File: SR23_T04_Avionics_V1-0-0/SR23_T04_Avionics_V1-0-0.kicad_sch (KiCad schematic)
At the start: 46 parts, among them J1 QWIIC, J11 Conn_01x02, J12 Conn_01x02, J13 Conn_01x02, J14 BAT_CHARGE, J2 QWIIC, J3 QWIIC, J4 BAT_POWER, J5 BAT_uC, J6 BAT_PCB+, J7 Conn_01x03, J8 Conn_01x03, J9 Conn_01x03, Q2 BSP75N, Q3 BSP75N, Q4 BSP75N, SW1 SW_DIP_x02, U1 MCP73831-2-OT, U2 MS563702BA03-50, U3 MPU-6050, U4 MOUDLE-SEEEDUINO-XIAO-ESP32C3

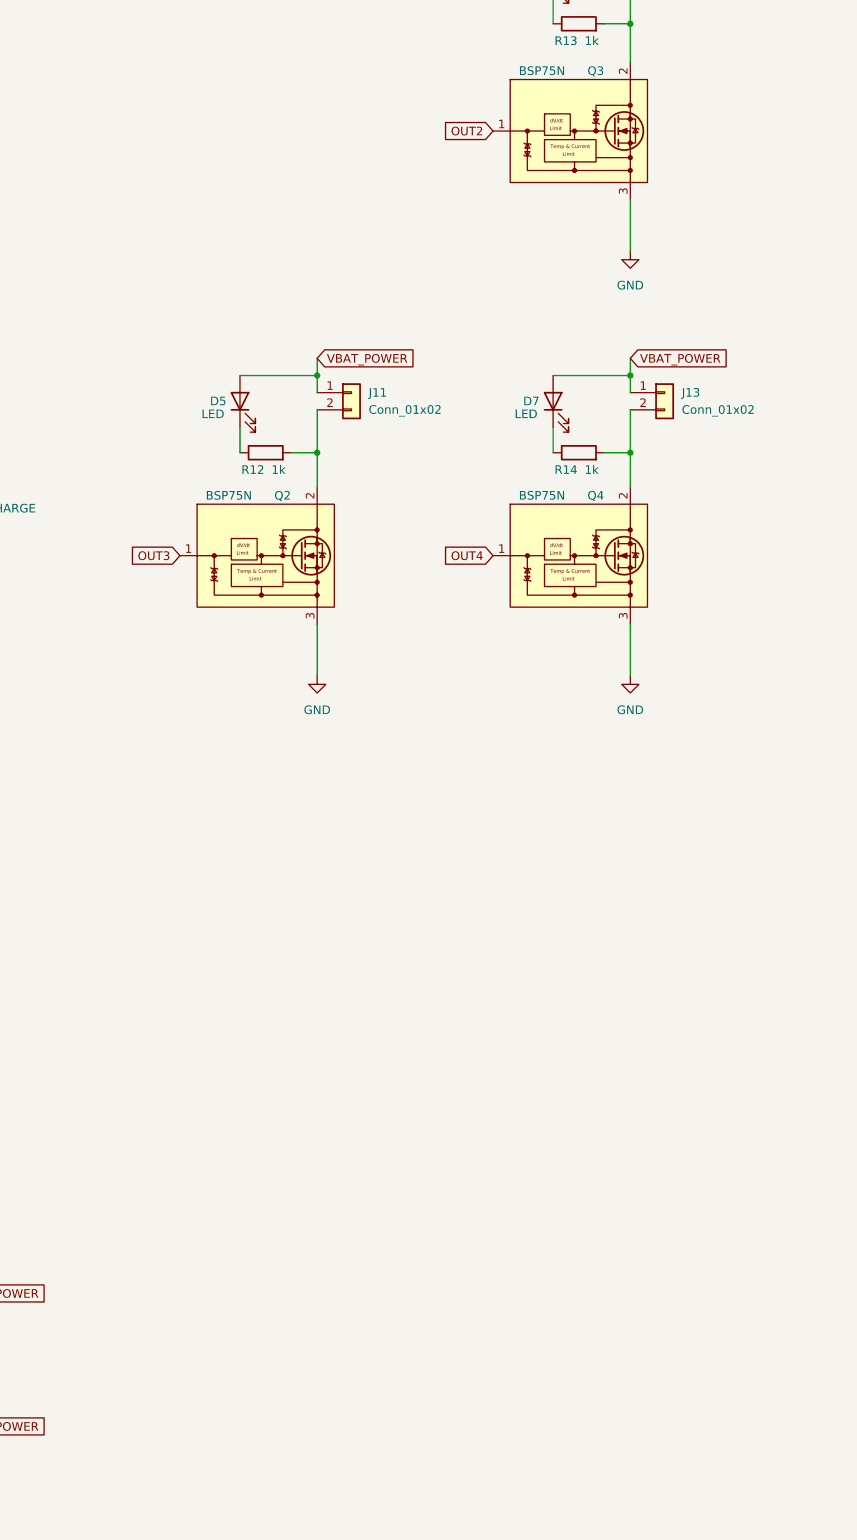
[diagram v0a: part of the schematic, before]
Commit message: wip: rooting of the board completed - waiting on review
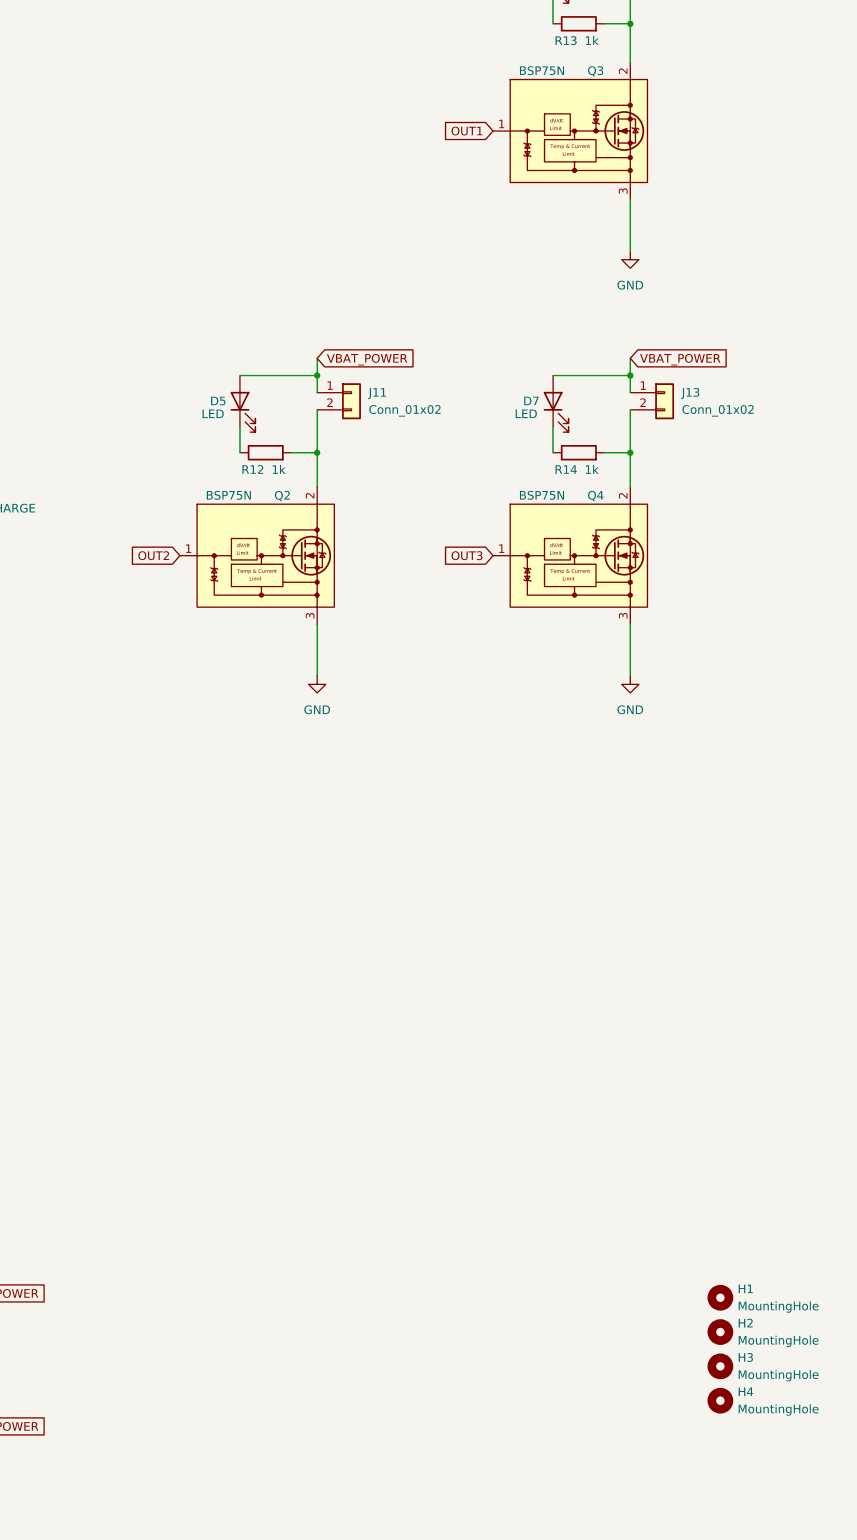
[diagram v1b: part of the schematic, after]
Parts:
- added H1, H2, H3, H4: MountingHole, MountingHole:MountingHole_3.2mm_M3_ISO7380, symbol Mechanical:MountingHole
- J14: footprint Connector_JST:JST_XH_S2B-XH-A-1_1x02_P2.50mm_Horizontal -> Connector_PinHeader_2.54mm:PinHeader_2x01_P2.54mm_Vertical
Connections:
- net OUT1: now also Q3.1 (G)
- net OUT2: now also Q2.1 (G); no longer Q3.1 (G)
- net OUT3: now also Q4.1 (G); no longer Q2.1 (G)
- net OUT4: no longer Q4.1 (G)
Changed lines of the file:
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@@
     )
   )
-  (global_label "OUT3" (shape input) (at 309.88 113.665 180) (fields_autoplaced)
+  (global_label "OUT2" (shape input) (at 309.88 113.665 180) (fields_autoplaced)
     (effects (font (size 1.27 1.27)) (justify right))
     (property "Intersheet References" "${INTERSHEET_REFS}" (id 0) (at 302.6288 113.5856 0)
@@
     )
   )
-  (global_label "OUT2" (shape input) (at 356.235 50.8 180) (fields_autoplaced)
+  (global_label "OUT1" (shape input) (at 356.235 50.8 180) (fields_autoplaced)
     (effects (font (size 1.27 1.27)) (justify right))
     (property "Intersheet References" "${INTERSHEET_REFS}" (id 0) (at 348.9838 50.7206 0)
@@
     )
   )
-  (global_label "OUT4" (shape input) (at 356.235 113.665 180) (fields_autoplaced)
+  (global_label "OUT3" (shape input) (at 356.235 113.665 180) (fields_autoplaced)
     (effects (font (size 1.27 1.27)) (justify right))
     (property "Intersheet References" "${INTERSHEET_REFS}" (id 0) (at 348.9838 113.5856 0)
@@
       (effects (font (size 1.27 1.27)) (justify right))
     )
-    (property "Footprint" "Connector_JST:JST_XH_S2B-XH-A-1_1x02_P2.50mm_Horizontal" (id 2) (at 271.78 105.41 0)
+    (property "Footprint" "Connector_PinHeader_2.54mm:PinHeader_2x01_P2.54mm_Vertical" (id 2) (at 271.78 105.41 0)
       (effects (font (size 1.27 1.27)) hide)
     )
@@
     (pin "1")
   )
+  (symbol (lib_id "Mechanical:MountingHole") (at 389.89 223.52 0) (unit 1)
+    (in_bom yes) (on_board yes) (fields_autoplaced)
+    (property "Reference" "H1" (id 0) (at 392.43 222.2499 0)
+      (effects (font (size 1.27 1.27)) (justify left))
+    )
+    (property "Value" "MountingHole" (id 1) (at 392.43 224.7899 0)
+      (effects (font (size 1.27 1.27)) (justify left))
+    )
+    (property "Footprint" "MountingHole:MountingHole_3.2mm_M3_ISO7380" (id 2) (at 389.89 223.52 0)
+      (effects (font (size 1.27 1.27)) hide)
+    )
+    (property "Datasheet" "~" (id 3) (at 389.89 223.52 0)
+      (effects (font (size 1.27 1.27)) hide)
+    )
+  )
   (symbol (lib_id "Connector_Generic:Conn_01x02") (at 175.26 199.39 90) (unit 1)
     (in_bom yes) (on_board yes) (fields_autoplaced)
@@
     (pin "1")
     (pin "2")
+  )
+  (symbol (lib_id "Mechanical:MountingHole") (at 389.89 228.6 0) (unit 1)
+    (in_bom yes) (on_board yes) (fields_autoplaced)
+    (property "Reference" "H2" (id 0) (at 392.43 227.3299 0)
+      (effects (font (size 1.27 1.27)) (justify left))
+    )
+    (property "Value" "MountingHole" (id 1) (at 392.43 229.8699 0)
+      (effects (font (size 1.27 1.27)) (justify left))
+    )
+    (property "Footprint" "MountingHole:MountingHole_3.2mm_M3_ISO7380" (id 2) (at 389.89 228.6 0)
+      (effects (font (size 1.27 1.27)) hide)
+    )
+    (property "Datasheet" "~" (id 3) (at 389.89 228.6 0)
+      (effects (font (size 1.27 1.27)) hide)
+    )
   )
   (symbol (lib_id "Device:R") (at 168.91 133.35 180) (unit 1)
@@
     (pin "2")
   )
+  (symbol (lib_id "Mechanical:MountingHole") (at 389.89 233.68 0) (unit 1)
+    (in_bom yes) (on_board yes) (fields_autoplaced)
+    (property "Reference" "H3" (id 0) (at 392.43 232.4099 0)
+      (effects (font (size 1.27 1.27)) (justify left))
+    )
+    (property "Value" "MountingHole" (id 1) (at 392.43 234.9499 0)
+      (effects (font (size 1.27 1.27)) (justify left))
+    )
+    (property "Footprint" "MountingHole:MountingHole_3.2mm_M3_ISO7380" (id 2) (at 389.89 233.68 0)
+      (effects (font (size 1.27 1.27)) hide)
+    )
+    (property "Datasheet" "~" (id 3) (at 389.89 233.68 0)
+      (effects (font (size 1.27 1.27)) hide)
+    )
+  )
   (symbol (lib_id "power:GND") (at 119.38 177.165 0) (unit 1)
     (in_bom yes) (on_board yes) (fields_autoplaced)
@@
     )
     (pin "1")
+  )
+  (symbol (lib_id "Mechanical:MountingHole") (at 389.89 238.76 0) (unit 1)
+    (in_bom yes) (on_board yes) (fields_autoplaced)
+    (property "Reference" "H4" (id 0) (at 392.43 237.4899 0)
+      (effects (font (size 1.27 1.27)) (justify left))
+    )
+    (property "Value" "MountingHole" (id 1) (at 392.43 240.0299 0)
+      (effects (font (size 1.27 1.27)) (justify left))
+    )
+    (property "Footprint" "MountingHole:MountingHole_3.2mm_M3_ISO7380" (id 2) (at 389.89 238.76 0)
+      (effects (font (size 1.27 1.27)) hide)
+    )
+    (property "Datasheet" "~" (id 3) (at 389.89 238.76 0)
+      (effects (font (size 1.27 1.27)) hide)
+    )
   )
   (symbol (lib_id "MS5037:MS563702BA03-50") (at 67.945 43.815 0) (unit 1)
@@
       (reference "D7") (unit 1) (value "LED") (footprint "LED_SMD:LED_0201_0603Metric_Pad0.64x0.40mm_HandSolder")
     )
+    (path "/298485de-c642-478c-8067-8a5d032e90c1"
+      (reference "H1") (unit 1) (value "MountingHole") (footprint "MountingHole:MountingHole_3.2mm_M3_ISO7380")
+    )
+    (path "/42218edd-ae1c-462d-a3bd-fe78546cce83"
+      (reference "H2") (unit 1) (value "MountingHole") (footprint "MountingHole:MountingHole_3.2mm_M3_ISO7380")
+    )
+    (path "/a2543711-4c28-4796-ba58-f8edb8d5c8d3"
+      (reference "H3") (unit 1) (value "MountingHole") (footprint "MountingHole:MountingHole_3.2mm_M3_ISO7380")
+    )
+    (path "/a91d7aa1-40e6-4d73-9d47-789fc8e6e41e"
+      (reference "H4") (unit 1) (value "MountingHole") (footprint "MountingHole:MountingHole_3.2mm_M3_ISO7380")
+    )
     (path "/05543cf1-c372-4ade-aa6a-9bc59abdadb7"
       (reference "J1") (unit 1) (value "QWIIC") (footprint "Connector_JST:JST_SH_SM04B-SRSS-TB_1x04-1MP_P1.00mm_Horizontal")
@@
     )
     (path "/01fa2a04-bc05-478d-a15d-fa035d52d7ba"
-      (reference "J14") (unit 1) (value "BAT_CHARGE") (footprint "Connector_JST:JST_XH_S2B-XH-A-1_1x02_P2.50mm_Horizontal")
+      (reference "J14") (unit 1) (value "BAT_CHARGE") (footprint "Connector_PinHeader_2.54mm:PinHeader_2x01_P2.54mm_Vertical")
     )
     (path "/521cdef5-5d04-4376-b227-1bb89aa93069"

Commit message: feat: Version 1.0.0 of the AV-Flow PCB
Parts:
- added D4: GREEN, LED_SMD:LED_0201_0603Metric_Pad0.64x0.40mm_HandSolder, symbol Device:LED
- added R11: 540, Resistor_SMD:R_0201_0603Metric_Pad0.64x0.40mm_HandSolder, symbol Device:R
- renumbered D6 to D5, D5 to D6, J3 to J1, J12 to J11, J11 to J12, J1 to J3, Q3 to Q1, Q4 to Q3, R13 to R12, R12 to R13
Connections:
- net GND: now also D4.1 (K)
- net OUT4: now also R11.1
- new net: D4.2 (A), R11.2

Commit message: wip: PCB V2
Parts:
- removed J11, J12, J13: Conn_01x02, Connector_JST:JST_PH_B2B-PH-K_1x02_P2.00mm_Vertical, symbol Connector_Generic:Conn_01x02
- added J10, J11, J12: Screw_Terminal_01x02, TerminalBlock_MetzConnect:TerminalBlock_MetzConnect_Type086_RT03402HBLC_1x02_P3.81mm_Horizontal, symbol Connector:Screw_Terminal_01x02
- C1, C2, C3, C4, C5, C6: footprint Capacitor_SMD:C_0201_0603Metric_Pad0.64x0.40mm_HandSolder -> Capacitor_SMD:C_0805_2012Metric_Pad1.18x1.45mm_HandSolder
- D1, D2, D3, D4, D5, D6, D7: footprint LED_SMD:LED_0201_0603Metric_Pad0.64x0.40mm_HandSolder -> LED_SMD:LED_0805_2012Metric_Pad1.15x1.40mm_HandSolder
- R1, R10, R11, R12, R13, R14, R2, R3, R4, R5, R6, R7, R8, R9: footprint Resistor_SMD:R_0201_0603Metric_Pad0.64x0.40mm_HandSolder -> Resistor_SMD:R_0805_2012Metric_Pad1.20x1.40mm_HandSolder
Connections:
- net DIP_1b: now also J10.1 (Pin_1), J11.1 (Pin_1), J12.1 (Pin_1)
- net OUT3: now also R11.1; no longer Q3.1 (G)
- net OUT4: now also Q3.1 (G); no longer R11.1
- net at Q3.2 (D), R14.2: now also J12.2 (Pin_2)
- net at Q1.2 (D), R12.2: now also J11.2 (Pin_2)
- net at Q2.2 (D), R13.2: now also J10.2 (Pin_2)

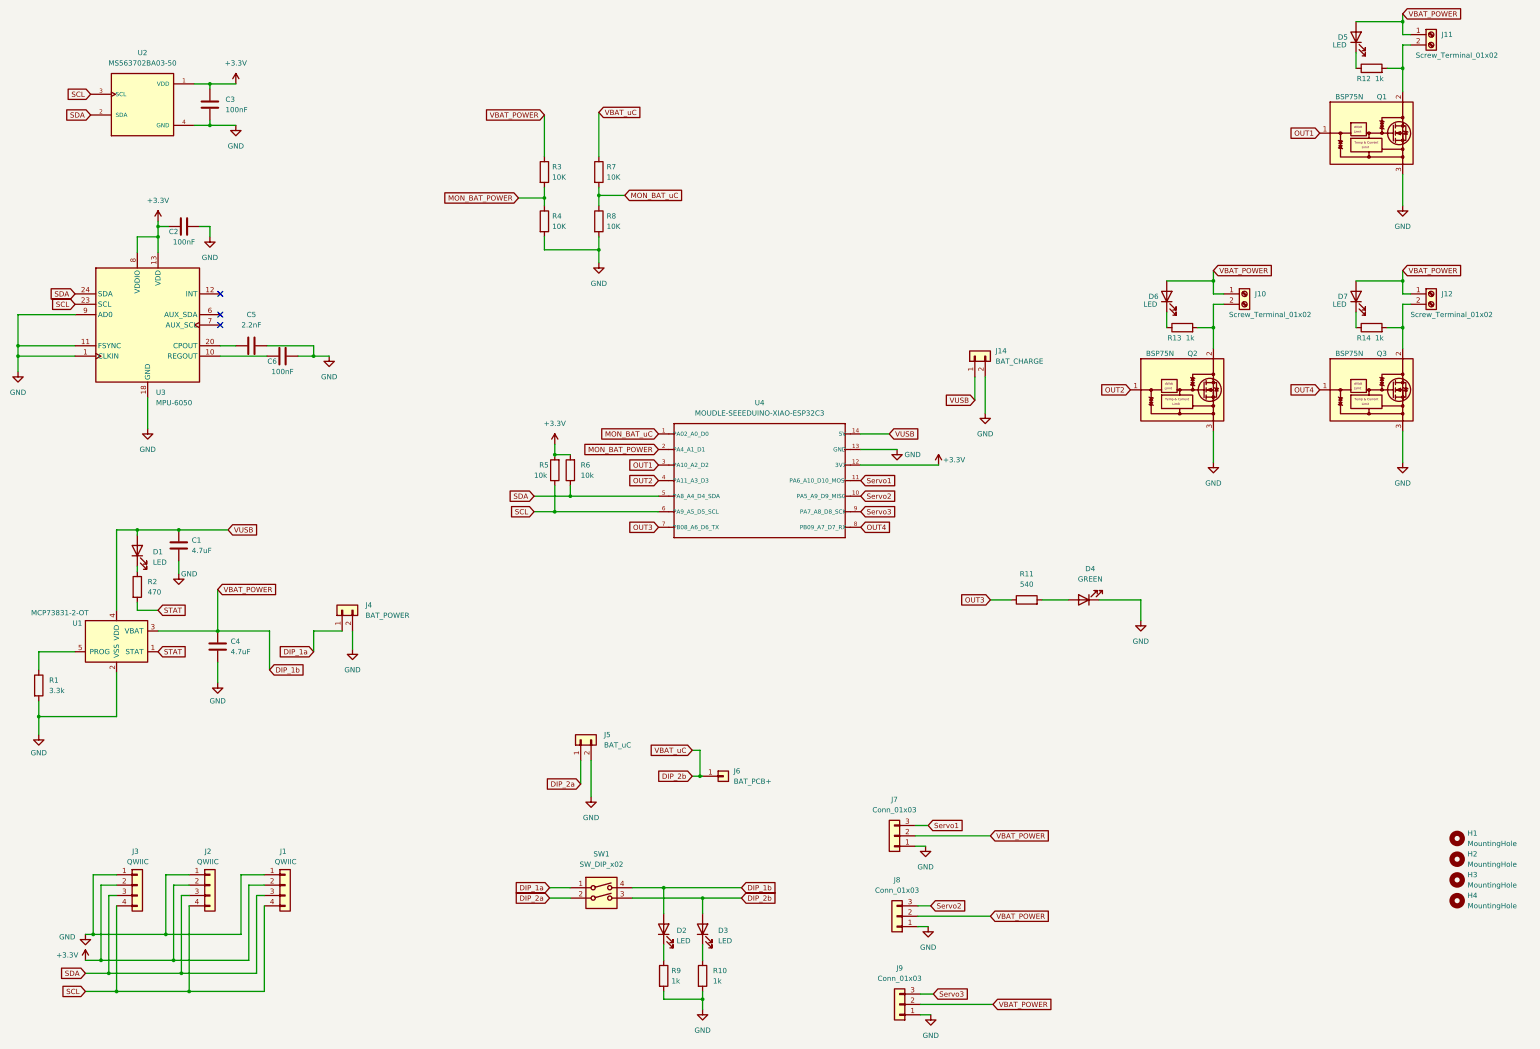
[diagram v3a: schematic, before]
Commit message: feat: new board V2 dual sided
closes: https://github.com/Hackuarium/Avionics/issues/7
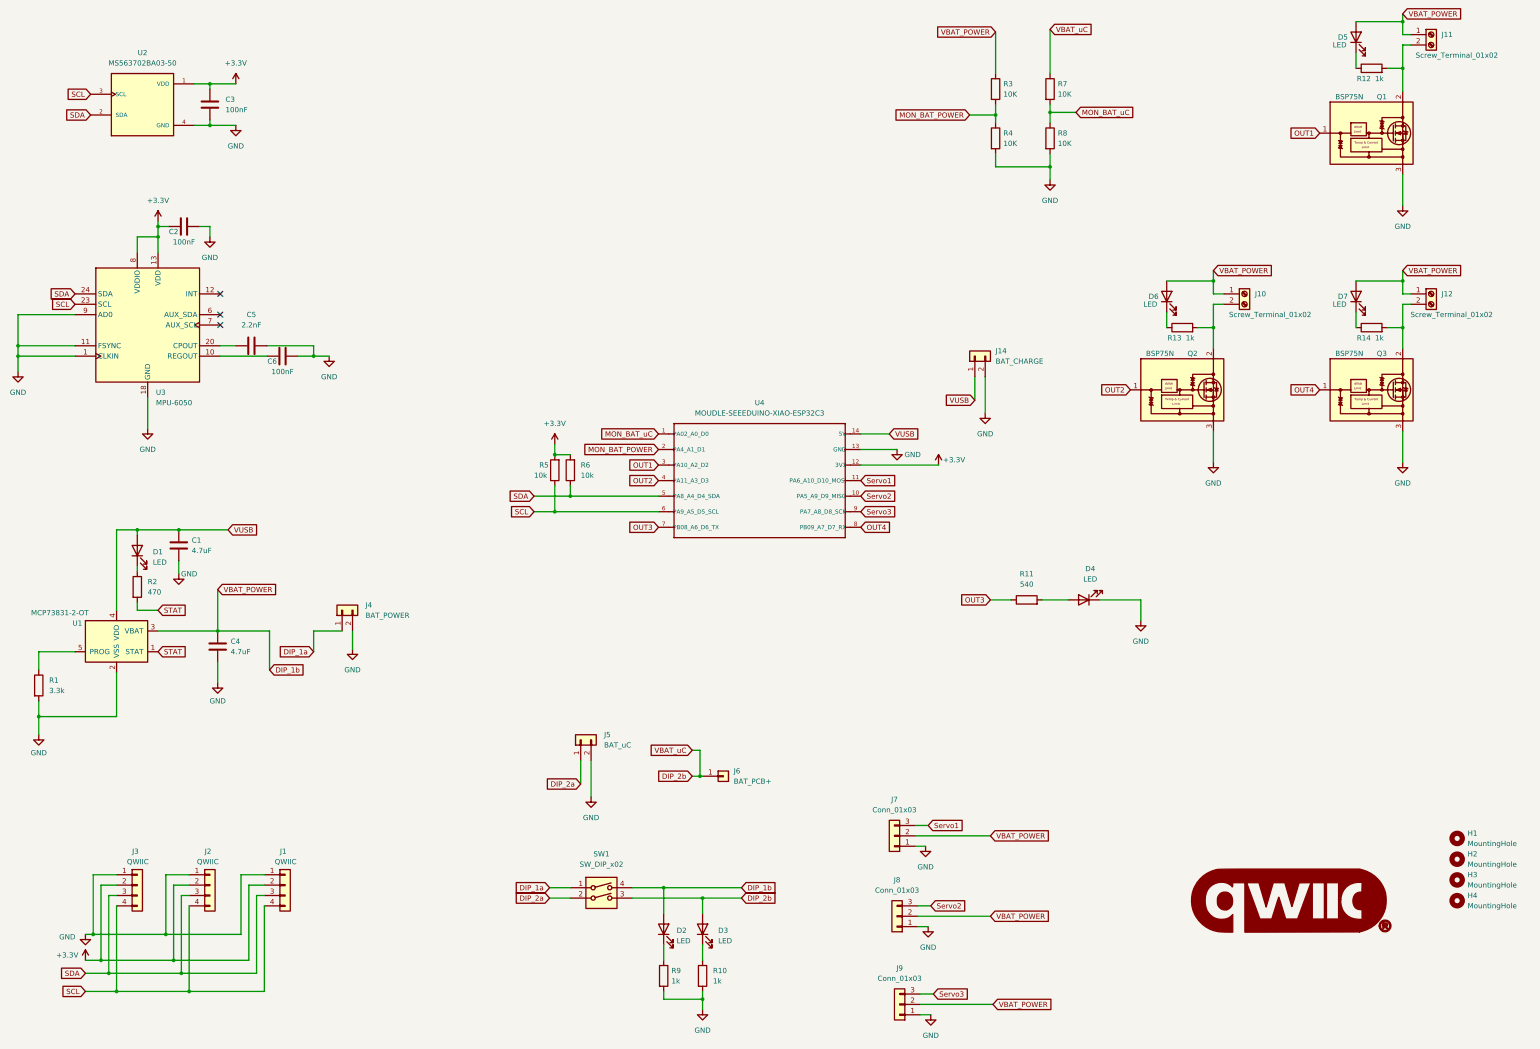
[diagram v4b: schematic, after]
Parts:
- D4: value GREEN -> LED
- SW1: footprint Button_Switch_THT:SW_DIP_SPSTx02_Slide_6.7x6.64mm_W7.62mm_P2.54mm_LowProfile -> Button_Switch_THT:SW_DIP_SPSTx02_Slide_9.78x7.26mm_W7.62mm_P2.54mm
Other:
- moved on the sheet: R3, R4, R7, R8
